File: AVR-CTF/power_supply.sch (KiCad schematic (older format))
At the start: 11 parts, among them J1 Conn_01x02, J2 Conn_01x03

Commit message: Esquematico para revision
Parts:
- gave numbers to parts that had none: 7
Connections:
- net labels added: VBUS
- net labels removed: 5VBUS, VDD
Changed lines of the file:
@@
 $EndDescr
 $Comp
-L Regulator_Linear:AMS1117-5.0 U?
+L Regulator_Linear:AMS1117-5.0 U1
 U 1 1 621012EE
 P 1850 1700
-F 0 "U?" H 1850 1942 50  0000 C CNN
+F 0 "U1" H 1850 1942 50  0000 C CNN
 F 1 "AMS1117-5.0" H 1850 1851 50  0000 C CNN
 F 2 "Package_TO_SOT_SMD:SOT-223-3_TabPin2" H 1850 1900 50  0001 C CNN
@@
 $EndComp
 $Comp
-L Device:C C?
+L Device:C C4
 U 1 1 621012F4
 P 2750 1850
-F 0 "C?" H 2865 1896 50  0000 L CNN
+F 0 "C4" H 2865 1896 50  0000 L CNN
 F 1 "10uF" H 2865 1805 50  0000 L CNN
 F 2 "Capacitor_SMD:C_0603_1608Metric_Pad1.08x0.95mm_HandSolder" H 2788 1700 50  0001 C CNN
@@
 $EndComp
 $Comp
-L Device:CP C?
+L Device:CP C1
 U 1 1 621012FA
 P 1250 1850
-F 0 "C?" H 1368 1896 50  0000 L CNN
+F 0 "C1" H 1368 1896 50  0000 L CNN
 F 1 "100uF" H 1368 1805 50  0000 L CNN
 F 2 "Capacitor_SMD:C_0805_2012Metric_Pad1.18x1.45mm_HandSolder" H 1288 1700 50  0001 C CNN
@@
 $EndComp
 $Comp
-L Device:CP C?
+L Device:CP C2
 U 1 1 62101300
 P 2300 1850
-F 0 "C?" H 2418 1896 50  0000 L CNN
+F 0 "C2" H 2418 1896 50  0000 L CNN
 F 1 "10uF" H 2418 1805 50  0000 L CNN
 F 2 "Capacitor_SMD:C_0805_2012Metric_Pad1.18x1.45mm_HandSolder" H 2338 1700 50  0001 C CNN
@@
 Connection ~ 2300 1700
 $Comp
-L power:GND #PWR?
+L power:GND #PWR05
 U 1 1 62101312
 P 1850 2000
-F 0 "#PWR?" H 1850 1750 50  0001 C CNN
+F 0 "#PWR05" H 1850 1750 50  0001 C CNN
 F 1 "GND" H 1855 1827 50  0000 C CNN
 F 2 "" H 1850 2000 50  0001 C CNN
@@
 Connection ~ 1925 3375
 $Comp
-L power:GND #PWR?
+L power:GND #PWR06
 U 1 1 62101319
 P 1925 3375
-F 0 "#PWR?" H 1925 3125 50  0001 C CNN
+F 0 "#PWR06" H 1925 3125 50  0001 C CNN
 F 1 "GND" H 1930 3202 50  0000 C CNN
 F 2 "" H 1925 3375 50  0001 C CNN
@@
 	2225 3075 2300 3075
 $Comp
-L Device:C C?
+L Device:C C5
 U 1 1 62101325
 P 2750 3225
-F 0 "C?" H 2865 3271 50  0000 L CNN
+F 0 "C5" H 2865 3271 50  0000 L CNN
 F 1 "10uF" H 2865 3180 50  0000 L CNN
 F 2 "Capacitor_SMD:C_0603_1608Metric_Pad1.08x0.95mm_HandSolder" H 2788 3075 50  0001 C CNN
@@
 $EndComp
 $Comp
-L Device:CP C?
+L Device:CP C3
 U 1 1 6210132B
 P 2300 3225
-F 0 "C?" H 2418 3271 50  0000 L CNN
+F 0 "C3" H 2418 3271 50  0000 L CNN
 F 1 "10uF" H 2418 3180 50  0000 L CNN
 F 2 "Capacitor_SMD:C_0805_2012Metric_Pad1.18x1.45mm_HandSolder" H 2338 3075 50  0001 C CNN
@@
 	1475 3075 1625 3075
 $Comp
-L Regulator_Linear:AMS1117-3.3 U?
+L Regulator_Linear:AMS1117-3.3 U2
 U 1 1 62101332
 P 1925 3075
-F 0 "U?" H 1925 3317 50  0000 C CNN
+F 0 "U2" H 1925 3317 50  0000 C CNN
 F 1 "AMS1117-3.3" H 1925 3226 50  0000 C CNN
 F 2 "Package_TO_SOT_SMD:SOT-223-3_TabPin2" H 1925 3275 50  0001 C CNN
@@
 3.3V POWER SUPPLY
 $Comp
-L power:+3.3V #PWR?
+L power:+3.3V #PWR07
 U 1 1 6210133B
 P 2750 3075
-F 0 "#PWR?" H 2750 2925 50  0001 C CNN
+F 0 "#PWR07" H 2750 2925 50  0001 C CNN
 F 1 "+3.3V" H 2765 3248 50  0000 C CNN
 F 2 "" H 2750 3075 50  0001 C CNN
@@
 Connection ~ 2750 3075
 $Comp
-L power:+5V #PWR?
+L power:+5V #PWR04
 U 1 1 62101342
 P 1475 3075
-F 0 "#PWR?" H 1475 2925 50  0001 C CNN
+F 0 "#PWR04" H 1475 2925 50  0001 C CNN
 F 1 "+5V" H 1475 3250 50  0000 C CNN
 F 2 "" H 1475 3075 50  0001 C CNN
@@
 AR Path="/621106C5" Ref="#PWR?"  Part="1"
 AR Path="/620E3406/621106C5" Ref="#PWR010"  Part="1"
-AR Path="/621FA25F/621106C5" Ref="#PWR?"  Part="1"
-F 0 "#PWR?" H 4375 3025 50  0001 C CNN
+AR Path="/621FA25F/621106C5" Ref="#PWR08"  Part="1"
+F 0 "#PWR08" H 4375 3025 50  0001 C CNN
 F 1 "+5V" V 4350 3350 50  0000 C CNN
 F 2 "" H 4375 3175 50  0001 C CNN
@@
 AR Path="/621106CB" Ref="J?"  Part="1"
 AR Path="/620E3406/621106CB" Ref="J2"  Part="1"
-AR Path="/621FA25F/621106CB" Ref="J?"  Part="1"
-F 0 "J?" H 4093 3492 50  0000 C CNN
+AR Path="/621FA25F/621106CB" Ref="J2"  Part="1"
+F 0 "J2" H 4093 3492 50  0000 C CNN
 F 1 "Conn_01x03" H 4093 3401 50  0000 C CNN
 F 2 "Connector_PinHeader_2.54mm:PinHeader_1x03_P2.54mm_Vertical" H 4175 3175 50  0001 C CNN
@@
 AR Path="/6211D42D" Ref="D?"  Part="1"
 AR Path="/620E3406/6211D42D" Ref="D3"  Part="1"
-AR Path="/621FA25F/6211D42D" Ref="D?"  Part="1"
-F 0 "D?" V 1168 4892 50  0000 C CNN
+AR Path="/621FA25F/6211D42D" Ref="D1"  Part="1"
+F 0 "D1" V 1168 4892 50  0000 C CNN
 F 1 "LED" V 1075 4875 50  0000 C CNN
 F 2 "LED_SMD:LED_0603_1608Metric_Pad1.05x0.95mm_HandSolder" H 1175 4675 50  0001 C CNN
@@
 AR Path="/6211D433" Ref="R?"  Part="1"
 AR Path="/620E3406/6211D433" Ref="R2"  Part="1"
-AR Path="/621FA25F/6211D433" Ref="R?"  Part="1"
-F 0 "R?" H 968 4375 50  0000 C CNN
+AR Path="/621FA25F/6211D433" Ref="R1"  Part="1"
+F 0 "R1" H 968 4375 50  0000 C CNN
 F 1 "1K" H 975 4275 50  0000 C CNN
 F 2 "Resistor_SMD:R_0603_1608Metric_Pad0.98x0.95mm_HandSolder" V 1105 4375 50  0001 C CNN
 F 3 "~" H 1175 4375 50  0001 C CNN
 	1    1175 4375
-	1    0    0    -1
-$EndComp
-$Comp
-L power:VDD #PWR?
-U 1 1 6211D439
-P 1175 4225
-AR Path="/6211D439" Ref="#PWR?"  Part="1"
-AR Path="/620E3406/6211D439" Ref="#PWR06"  Part="1"
-AR Path="/621FA25F/6211D439" Ref="#PWR?"  Part="1"
-F 0 "#PWR?" H 1175 4075 50  0001 C CNN
-F 1 "VDD" H 1075 4375 50  0000 L CNN
-F 2 "" H 1175 4225 50  0001 C CNN
-F 3 "" H 1175 4225 50  0001 C CNN
-	1    1175 4225
 	1    0    0    -1
 $EndComp
@@
 AR Path="/6211D43F" Ref="#PWR?"  Part="1"
 AR Path="/620E3406/6211D43F" Ref="#PWR07"  Part="1"
-AR Path="/621FA25F/6211D43F" Ref="#PWR?"  Part="1"
-F 0 "#PWR?" H 1175 4575 50  0001 C CNN
+AR Path="/621FA25F/6211D43F" Ref="#PWR02"  Part="1"
+F 0 "#PWR02" H 1175 4575 50  0001 C CNN
 F 1 "GND" H 1175 4675 50  0000 R CNN
 F 2 "" H 1175 4825 50  0001 C CNN
@@
 AR Path="/621350E1" Ref="#PWR?"  Part="1"
 AR Path="/620E3406/621350E1" Ref="#PWR011"  Part="1"
-AR Path="/621FA25F/621350E1" Ref="#PWR?"  Part="1"
-F 0 "#PWR?" H 4400 1700 50  0001 C CNN
+AR Path="/621FA25F/621350E1" Ref="#PWR09"  Part="1"
+F 0 "#PWR09" H 4400 1700 50  0001 C CNN
 F 1 "GND" H 4475 1775 50  0000 R CNN
 F 2 "" H 4400 1950 50  0001 C CNN
@@
 AR Path="/621350E7" Ref="J?"  Part="1"
 AR Path="/620E3406/621350E7" Ref="J1"  Part="1"
-AR Path="/621FA25F/621350E7" Ref="J?"  Part="1"
-F 0 "J?" H 4043 1575 50  0000 C CNN
+AR Path="/621FA25F/621350E7" Ref="J1"  Part="1"
+F 0 "J1" H 4043 1575 50  0000 C CNN
 F 1 "Conn_01x02" H 4043 1666 50  0000 C CNN
 F 2 "Connector_PinHeader_2.54mm:PinHeader_1x02_P2.54mm_Vertical" H 4125 1900 50  0001 C CNN
@@
 Connection ~ 1250 1700
 $Comp
-L power:+12V #PWR?
+L power:+12V #PWR03
 U 1 1 62124F62
 P 1250 1700
-F 0 "#PWR?" H 1250 1550 50  0001 C CNN
+F 0 "#PWR03" H 1250 1550 50  0001 C CNN
 F 1 "+12V" H 1265 1873 50  0000 C CNN
 F 2 "" H 1250 1700 50  0001 C CNN
@@
 	1550 1700 1250 1700
 Text HLabel 4700 3075 2    50   Input ~ 0
-5VBUS
+VBUS
 Wire Notes Line
 	800  2500 3100 2500
@@
 	4400 1900 4400 1950
 $Comp
-L power:GND1 #PWR?
+L power:GND1 #PWR010
 U 1 1 6220336F
 P 4625 1950
-F 0 "#PWR?" H 4625 1700 50  0001 C CNN
+F 0 "#PWR010" H 4625 1700 50  0001 C CNN
 F 1 "GND1" H 4630 1777 50  0000 C CNN
 F 2 "" H 4625 1950 50  0001 C CNN
@@
 Wire Wire Line
 	4325 1800 4625 1800
+$Comp
+L power:+5V #PWR0105
+U 1 1 62750FD7
+P 1175 4225
+F 0 "#PWR0105" H 1175 4075 50  0001 C CNN
+F 1 "+5V" H 1175 4400 50  0000 C CNN
+F 2 "" H 1175 4225 50  0001 C CNN
+F 3 "" H 1175 4225 50  0001 C CNN
+	1    1175 4225
+	1    0    0    -1
+$EndComp
 $EndSCHEMATC

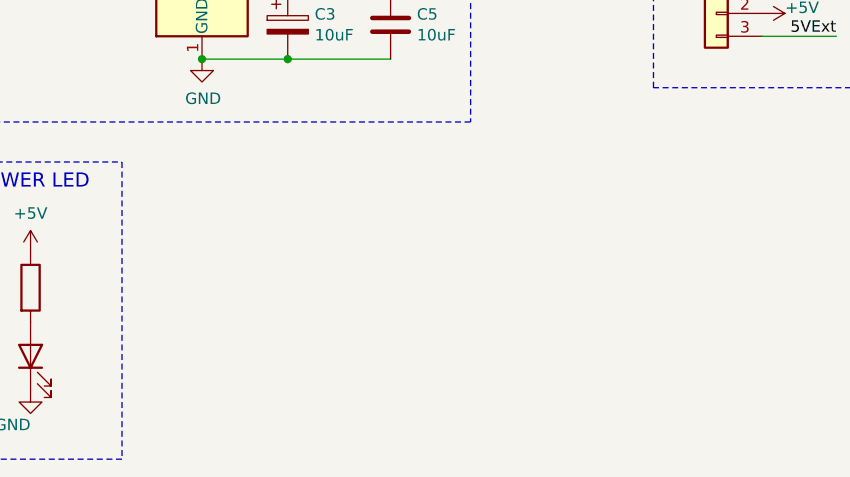
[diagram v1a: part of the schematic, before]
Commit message: Regulador de voltaje adicional para el avr-ctf
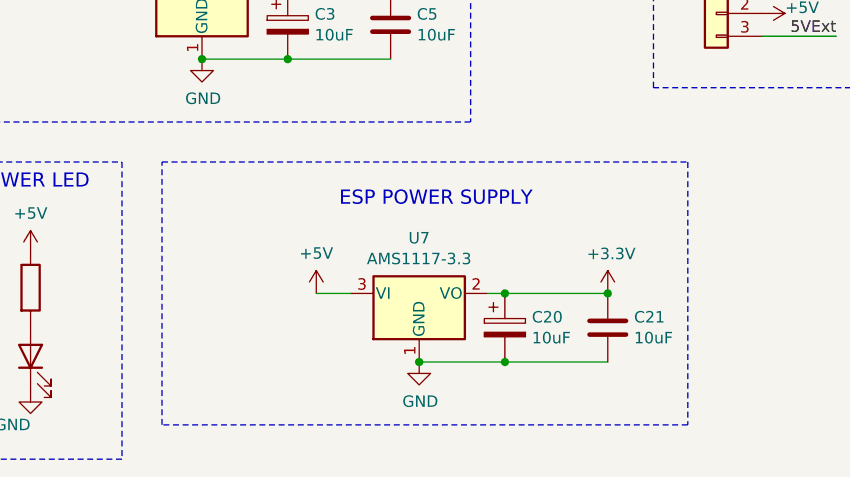
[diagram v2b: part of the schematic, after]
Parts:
- added C20: 10uF, Capacitor_SMD:C_0805_2012Metric_Pad1.18x1.45mm_HandSolder, symbol Device:CP
- added C21: 10uF, Capacitor_SMD:C_0603_1608Metric_Pad1.08x0.95mm_HandSolder, symbol Device:C
- added U7: AMS1117-3.3, Package_TO_SOT_SMD:SOT-223-3_TabPin2, symbol Regulator_Linear:AMS1117-3.3
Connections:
- wire segments 17 -> 22
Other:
- note added: "ESP POWER SUPPLY"
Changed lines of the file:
@@
 	1    0    0    -1
 $EndComp
+Connection ~ 2875 4700
+$Comp
+L power:GND #PWR011
+U 1 1 6278C8CD
+P 2875 4700
+F 0 "#PWR011" H 2875 4450 50  0001 C CNN
+F 1 "GND" H 2880 4527 50  0000 C CNN
+F 2 "" H 2875 4700 50  0001 C CNN
+F 3 "" H 2875 4700 50  0001 C CNN
+	1    2875 4700
+	1    0    0    -1
+$EndComp
+Connection ~ 3250 4700
+Wire Wire Line
+	3250 4700 3700 4700
+Wire Wire Line
+	2875 4700 3250 4700
+Connection ~ 3250 4400
+Wire Wire Line
+	3250 4400 3700 4400
+Wire Wire Line
+	3175 4400 3250 4400
+$Comp
+L Device:C C21
+U 1 1 6278C8D9
+P 3700 4550
+F 0 "C21" H 3815 4596 50  0000 L CNN
+F 1 "10uF" H 3815 4505 50  0000 L CNN
+F 2 "Capacitor_SMD:C_0603_1608Metric_Pad1.08x0.95mm_HandSolder" H 3738 4400 50  0001 C CNN
+F 3 "~" H 3700 4550 50  0001 C CNN
+	1    3700 4550
+	1    0    0    -1
+$EndComp
+$Comp
+L Device:CP C20
+U 1 1 6278C8DF
+P 3250 4550
+F 0 "C20" H 3368 4596 50  0000 L CNN
+F 1 "10uF" H 3368 4505 50  0000 L CNN
+F 2 "Capacitor_SMD:C_0805_2012Metric_Pad1.18x1.45mm_HandSolder" H 3288 4400 50  0001 C CNN
+F 3 "~" H 3250 4550 50  0001 C CNN
+	1    3250 4550
+	1    0    0    -1
+$EndComp
+Wire Wire Line
+	2425 4400 2575 4400
+$Comp
+L Regulator_Linear:AMS1117-3.3 U7
+U 1 1 6278C8E6
+P 2875 4400
+F 0 "U7" H 2875 4642 50  0000 C CNN
+F 1 "AMS1117-3.3" H 2875 4551 50  0000 C CNN
+F 2 "Package_TO_SOT_SMD:SOT-223-3_TabPin2" H 2875 4600 50  0001 C CNN
+F 3 "http://www.advanced-monolithic.com/pdf/ds1117.pdf" H 2975 4150 50  0001 C CNN
+	1    2875 4400
+	1    0    0    -1
+$EndComp
+Text Notes 2525 4025 0    62   ~ 0
+ESP POWER SUPPLY
+$Comp
+L power:+5V #PWR01
+U 1 1 6278C8F4
+P 2425 4400
+F 0 "#PWR01" H 2425 4250 50  0001 C CNN
+F 1 "+5V" H 2425 4575 50  0000 C CNN
+F 2 "" H 2425 4400 50  0001 C CNN
+F 3 "" H 2425 4400 50  0001 C CNN
+	1    2425 4400
+	1    0    0    -1
+$EndComp
+Wire Notes Line
+	1750 3825 4050 3825
+Wire Notes Line
+	4050 3825 4050 4975
+Wire Notes Line
+	4050 4975 1750 4975
+Wire Notes Line
+	1750 4975 1750 3825
+$Comp
+L power:+3.3V #PWR012
+U 1 1 627A1439
+P 3700 4400
+F 0 "#PWR012" H 3700 4250 50  0001 C CNN
+F 1 "+3.3V" H 3715 4573 50  0000 C CNN
+F 2 "" H 3700 4400 50  0001 C CNN
+F 3 "" H 3700 4400 50  0001 C CNN
+	1    3700 4400
+	1    0    0    -1
+$EndComp
+Connection ~ 3700 4400
 $EndSCHEMATC

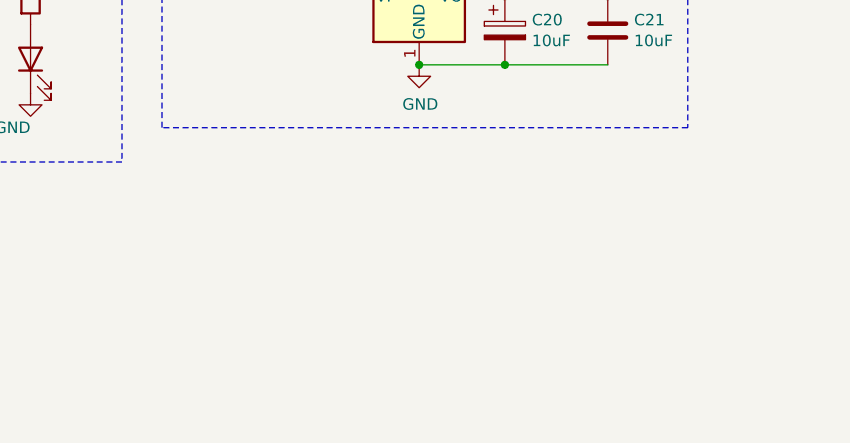
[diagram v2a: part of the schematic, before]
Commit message: Anexo de otro FTDI y regulador de voltaje
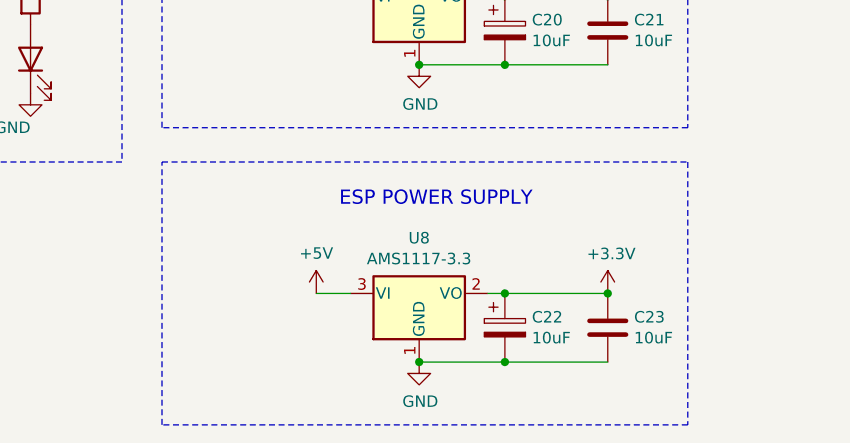
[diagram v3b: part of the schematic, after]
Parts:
- added C22: 10uF, Capacitor_SMD:C_0805_2012Metric_Pad1.18x1.45mm_HandSolder, symbol Device:CP
- added C23: 10uF, Capacitor_SMD:C_0603_1608Metric_Pad1.08x0.95mm_HandSolder, symbol Device:C
- added U8: AMS1117-3.3, Package_TO_SOT_SMD:SOT-223-3_TabPin2, symbol Regulator_Linear:AMS1117-3.3
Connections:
- wire segments 22 -> 27
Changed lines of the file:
@@
 $EndComp
 Connection ~ 3700 4400
+Connection ~ 2875 6000
+$Comp
+L power:GND #PWR016
+U 1 1 62322E8A
+P 2875 6000
+F 0 "#PWR016" H 2875 5750 50  0001 C CNN
+F 1 "GND" H 2880 5827 50  0000 C CNN
+F 2 "" H 2875 6000 50  0001 C CNN
+F 3 "" H 2875 6000 50  0001 C CNN
+	1    2875 6000
+	1    0    0    -1
+$EndComp
+Connection ~ 3250 6000
+Wire Wire Line
+	3250 6000 3700 6000
+Wire Wire Line
+	2875 6000 3250 6000
+Connection ~ 3250 5700
+Wire Wire Line
+	3250 5700 3700 5700
+Wire Wire Line
+	3175 5700 3250 5700
+$Comp
+L Device:C C23
+U 1 1 62322E96
+P 3700 5850
+F 0 "C23" H 3815 5896 50  0000 L CNN
+F 1 "10uF" H 3815 5805 50  0000 L CNN
+F 2 "Capacitor_SMD:C_0603_1608Metric_Pad1.08x0.95mm_HandSolder" H 3738 5700 50  0001 C CNN
+F 3 "~" H 3700 5850 50  0001 C CNN
+	1    3700 5850
+	1    0    0    -1
+$EndComp
+$Comp
+L Device:CP C22
+U 1 1 62322E9C
+P 3250 5850
+F 0 "C22" H 3368 5896 50  0000 L CNN
+F 1 "10uF" H 3368 5805 50  0000 L CNN
+F 2 "Capacitor_SMD:C_0805_2012Metric_Pad1.18x1.45mm_HandSolder" H 3288 5700 50  0001 C CNN
+F 3 "~" H 3250 5850 50  0001 C CNN
+	1    3250 5850
+	1    0    0    -1
+$EndComp
+Wire Wire Line
+	2425 5700 2575 5700
+$Comp
+L Regulator_Linear:AMS1117-3.3 U8
+U 1 1 62322EA3
+P 2875 5700
+F 0 "U8" H 2875 5942 50  0000 C CNN
+F 1 "AMS1117-3.3" H 2875 5851 50  0000 C CNN
+F 2 "Package_TO_SOT_SMD:SOT-223-3_TabPin2" H 2875 5900 50  0001 C CNN
+F 3 "http://www.advanced-monolithic.com/pdf/ds1117.pdf" H 2975 5450 50  0001 C CNN
+	1    2875 5700
+	1    0    0    -1
+$EndComp
+Text Notes 2525 5325 0    62   ~ 0
+ESP POWER SUPPLY
+$Comp
+L power:+5V #PWR013
+U 1 1 62322EB1
+P 2425 5700
+F 0 "#PWR013" H 2425 5550 50  0001 C CNN
+F 1 "+5V" H 2425 5875 50  0000 C CNN
+F 2 "" H 2425 5700 50  0001 C CNN
+F 3 "" H 2425 5700 50  0001 C CNN
+	1    2425 5700
+	1    0    0    -1
+$EndComp
+Wire Notes Line
+	1750 5125 4050 5125
+Wire Notes Line
+	4050 5125 4050 6275
+Wire Notes Line
+	4050 6275 1750 6275
+Wire Notes Line
+	1750 6275 1750 5125
+$Comp
+L power:+3.3V #PWR018
+U 1 1 62323DD7
+P 3700 5700
+F 0 "#PWR018" H 3700 5550 50  0001 C CNN
+F 1 "+3.3V" H 3715 5873 50  0000 C CNN
+F 2 "" H 3700 5700 50  0001 C CNN
+F 3 "" H 3700 5700 50  0001 C CNN
+	1    3700 5700
+	1    0    0    -1
+$EndComp
+Connection ~ 3700 5700
 $EndSCHEMATC

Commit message: Versión para revisión
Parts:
- removed C22: 10uF, Capacitor_SMD:C_0805_2012Metric_Pad1.18x1.45mm_HandSolder, symbol Device:CP
- removed C23: 10uF, Capacitor_SMD:C_0603_1608Metric_Pad1.08x0.95mm_HandSolder, symbol Device:C
- removed U8: AMS1117-3.3, Package_TO_SOT_SMD:SOT-223-3_TabPin2, symbol Regulator_Linear:AMS1117-3.3
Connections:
- wire segments 27 -> 22
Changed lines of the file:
@@
 $EndComp
 Connection ~ 3700 4400
-Connection ~ 2875 6000
-$Comp
-L power:GND #PWR016
-U 1 1 62322E8A
-P 2875 6000
-F 0 "#PWR016" H 2875 5750 50  0001 C CNN
-F 1 "GND" H 2880 5827 50  0000 C CNN
-F 2 "" H 2875 6000 50  0001 C CNN
-F 3 "" H 2875 6000 50  0001 C CNN
-	1    2875 6000
-	1    0    0    -1
-$EndComp
-Connection ~ 3250 6000
-Wire Wire Line
-	3250 6000 3700 6000
-Wire Wire Line
-	2875 6000 3250 6000
-Connection ~ 3250 5700
-Wire Wire Line
-	3250 5700 3700 5700
-Wire Wire Line
-	3175 5700 3250 5700
-$Comp
-L Device:C C23
-U 1 1 62322E96
-P 3700 5850
-F 0 "C23" H 3815 5896 50  0000 L CNN
-F 1 "10uF" H 3815 5805 50  0000 L CNN
-F 2 "Capacitor_SMD:C_0603_1608Metric_Pad1.08x0.95mm_HandSolder" H 3738 5700 50  0001 C CNN
-F 3 "~" H 3700 5850 50  0001 C CNN
-	1    3700 5850
-	1    0    0    -1
-$EndComp
-$Comp
-L Device:CP C22
-U 1 1 62322E9C
-P 3250 5850
-F 0 "C22" H 3368 5896 50  0000 L CNN
-F 1 "10uF" H 3368 5805 50  0000 L CNN
-F 2 "Capacitor_SMD:C_0805_2012Metric_Pad1.18x1.45mm_HandSolder" H 3288 5700 50  0001 C CNN
-F 3 "~" H 3250 5850 50  0001 C CNN
-	1    3250 5850
-	1    0    0    -1
-$EndComp
-Wire Wire Line
-	2425 5700 2575 5700
-$Comp
-L Regulator_Linear:AMS1117-3.3 U8
-U 1 1 62322EA3
-P 2875 5700
-F 0 "U8" H 2875 5942 50  0000 C CNN
-F 1 "AMS1117-3.3" H 2875 5851 50  0000 C CNN
-F 2 "Package_TO_SOT_SMD:SOT-223-3_TabPin2" H 2875 5900 50  0001 C CNN
-F 3 "http://www.advanced-monolithic.com/pdf/ds1117.pdf" H 2975 5450 50  0001 C CNN
-	1    2875 5700
-	1    0    0    -1
-$EndComp
-Text Notes 2525 5325 0    62   ~ 0
-ESP POWER SUPPLY
-$Comp
-L power:+5V #PWR013
-U 1 1 62322EB1
-P 2425 5700
-F 0 "#PWR013" H 2425 5550 50  0001 C CNN
-F 1 "+5V" H 2425 5875 50  0000 C CNN
-F 2 "" H 2425 5700 50  0001 C CNN
-F 3 "" H 2425 5700 50  0001 C CNN
-	1    2425 5700
-	1    0    0    -1
-$EndComp
-Wire Notes Line
-	1750 5125 4050 5125
-Wire Notes Line
-	4050 5125 4050 6275
-Wire Notes Line
-	4050 6275 1750 6275
-Wire Notes Line
-	1750 6275 1750 5125
-$Comp
-L power:+3.3V #PWR018
-U 1 1 62323DD7
-P 3700 5700
-F 0 "#PWR018" H 3700 5550 50  0001 C CNN
-F 1 "+3.3V" H 3715 5873 50  0000 C CNN
-F 2 "" H 3700 5700 50  0001 C CNN
-F 3 "" H 3700 5700 50  0001 C CNN
-	1    3700 5700
-	1    0    0    -1
-$EndComp
-Connection ~ 3700 5700
 $EndSCHEMATC

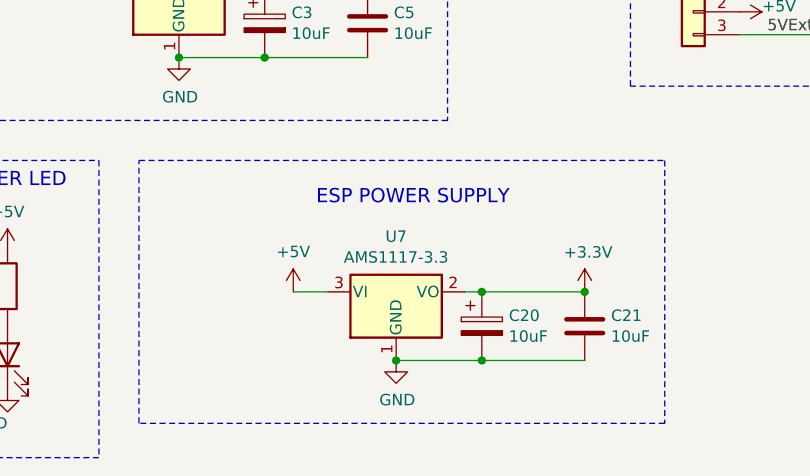
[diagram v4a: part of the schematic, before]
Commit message: Generacion de gerbers y boom agrupado
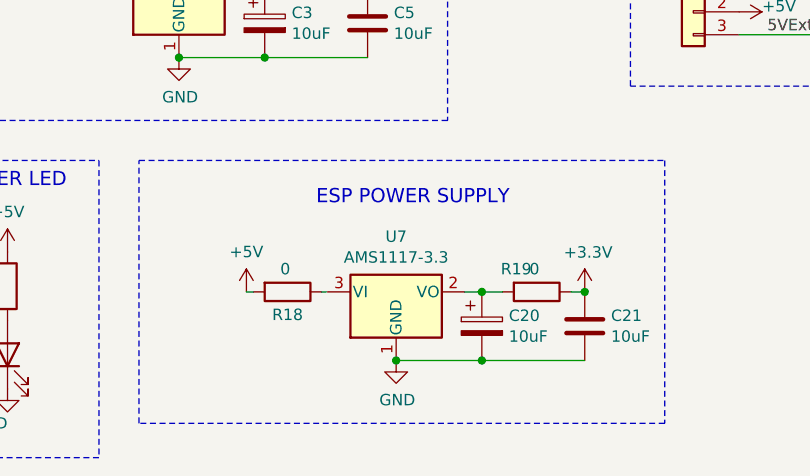
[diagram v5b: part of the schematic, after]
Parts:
- added R18, R19: 0, Resistor_SMD:R_0603_1608Metric_Pad0.98x0.95mm_HandSolder, symbol Device:R
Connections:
- wire segments 22 -> 24
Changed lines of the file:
@@
 Wire Wire Line
 	2875 4700 3250 4700
-Connection ~ 3250 4400
-Wire Wire Line
-	3250 4400 3700 4400
 Wire Wire Line
 	3175 4400 3250 4400
@@
 	1    0    0    -1
 $EndComp
-Wire Wire Line
-	2425 4400 2575 4400
 $Comp
 L Regulator_Linear:AMS1117-3.3 U7
@@
 L power:+5V #PWR01
 U 1 1 6278C8F4
-P 2425 4400
-F 0 "#PWR01" H 2425 4250 50  0001 C CNN
-F 1 "+5V" H 2425 4575 50  0000 C CNN
-F 2 "" H 2425 4400 50  0001 C CNN
-F 3 "" H 2425 4400 50  0001 C CNN
-	1    2425 4400
+P 2220 4400
+F 0 "#PWR01" H 2220 4250 50  0001 C CNN
+F 1 "+5V" H 2220 4575 50  0000 C CNN
+F 2 "" H 2220 4400 50  0001 C CNN
+F 3 "" H 2220 4400 50  0001 C CNN
+	1    2220 4400
 	1    0    0    -1
 $EndComp
@@
 	1    0    0    -1
 $EndComp
+$Comp
+L Device:R R?
+U 1 1 62350913
+P 2400 4400
+AR Path="/62350913" Ref="R?"  Part="1"
+AR Path="/620E3406/62350913" Ref="R?"  Part="1"
+AR Path="/621FA25F/62350913" Ref="R18"  Part="1"
+F 0 "R18" V 2500 4400 50  0000 C CNN
+F 1 "0" V 2300 4390 50  0000 C CNN
+F 2 "Resistor_SMD:R_0603_1608Metric_Pad0.98x0.95mm_HandSolder" V 2330 4400 50  0001 C CNN
+F 3 "~" H 2400 4400 50  0001 C CNN
+	1    2400 4400
+	0    1    1    0
+$EndComp
+Wire Wire Line
+	2570 4400 2550 4400
+Wire Wire Line
+	2250 4400 2220 4400
+$Comp
+L Device:R R?
+U 1 1 6235288C
+P 3490 4400
+AR Path="/6235288C" Ref="R?"  Part="1"
+AR Path="/620E3406/6235288C" Ref="R?"  Part="1"
+AR Path="/621FA25F/6235288C" Ref="R19"  Part="1"
+F 0 "R19" V 3390 4310 50  0000 C CNN
+F 1 "0" V 3390 4390 50  0000 C CNN
+F 2 "Resistor_SMD:R_0603_1608Metric_Pad0.98x0.95mm_HandSolder" V 3420 4400 50  0001 C CNN
+F 3 "~" H 3490 4400 50  0001 C CNN
+	1    3490 4400
+	0    1    1    0
+$EndComp
+Wire Wire Line
+	3250 4400 3340 4400
+Connection ~ 3250 4400
+Wire Wire Line
+	3640 4400 3700 4400
 Connection ~ 3700 4400
 $EndSCHEMATC
